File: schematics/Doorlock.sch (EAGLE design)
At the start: 40 parts, among them IC1 AT90S2313S, K1 G5V1, K2 G5V1, X1 RASPI_BOARD_B+#_H, X2 RIA182-04, X3 RIA182-07, X4 RIA182-05

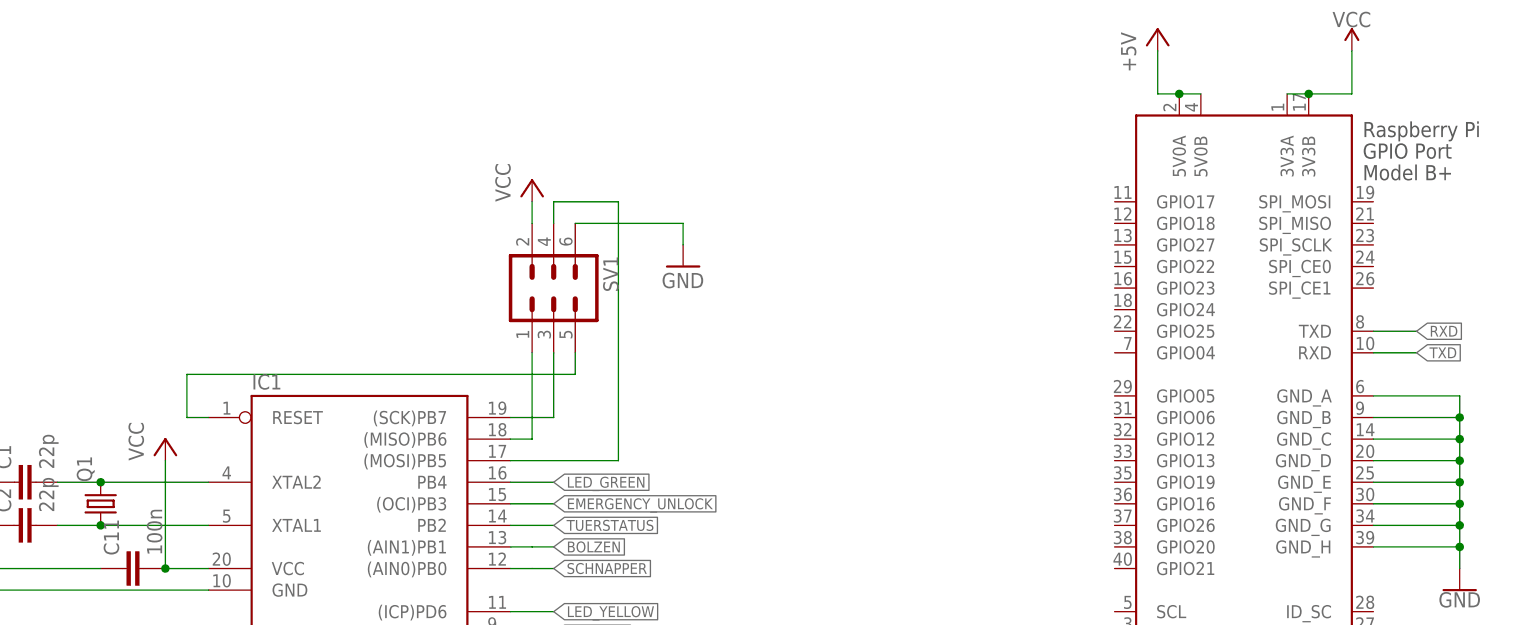
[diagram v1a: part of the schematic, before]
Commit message: Remove ISP adapter
Let's flash the device with the Raspberry Pi :-)
... But add an Jumper for the reset line.

Signed-off-by: Ralf Ramsauer <ralf@binary-kitchen.de>
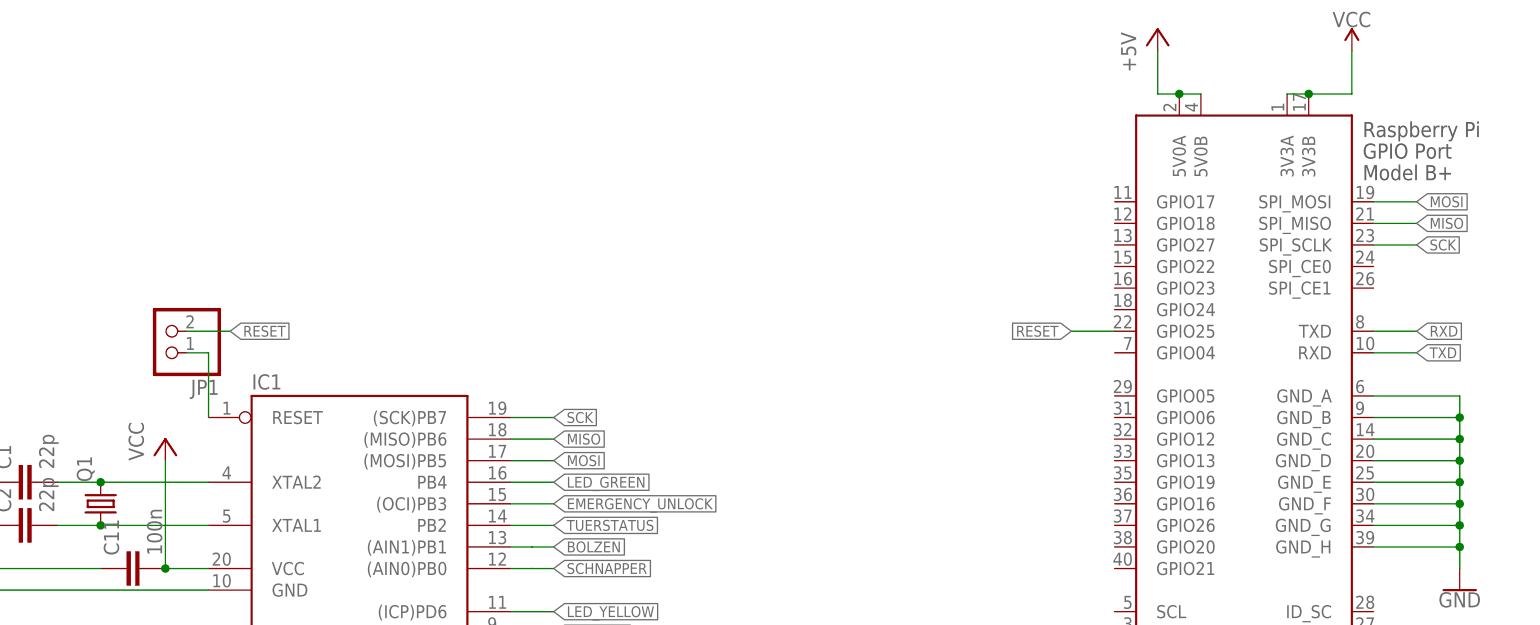
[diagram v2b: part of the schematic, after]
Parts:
- removed SV1: (no value), con-harting-ml:ML6
- added JP1: (no value), pinhead:PINHD-1X2
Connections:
- removed net N$2: IC1.(SCK)PB7, SV1.3
- removed net N$3: IC1.RESET, SV1.5
- removed net N$5: IC1.(MOSI)PB5, SV1.4
- new net MISO: IC1.(MISO)PB6, X1.SPI_MISO
- new net MOSI: IC1.(MOSI)PB5, X1.SPI_MOSI
- new net RESET: JP1.2, X1.GPIO25
- new net SCK: IC1.(SCK)PB7, X1.SPI_SCLK
- net GND: no longer SV1.6
- net N$1: now also IC1.RESET, JP1.1; no longer IC1.(MISO)PB6, SV1.1
- net VCC: no longer SV1.2
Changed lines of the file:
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@@
 <?xml version="1.0" encoding="utf-8"?>
 <!DOCTYPE eagle SYSTEM "eagle.dtd">
-<eagle version="9.1.2">
+<eagle version="9.1.3">
 <drawing>
 <settings>
@@
 <parts>
 <part name="IC1" library="atmel" deviceset="AT90S2313" device="S" value="AT90S2313S"/>
-<part name="SV1" library="con-harting-ml" deviceset="ML6" device=""/>
-<part name="GND1" library="supply1" deviceset="GND" device=""/>
-<part name="P+1" library="supply1" deviceset="VCC" device=""/>
 <part name="Q1" library="crystal" deviceset="CRYSTAL" device="HC49UP"/>
 <part name="C1" library="rcl" deviceset="C-EU" device="C0805" value="22p"/>
@@
 <part name="LED1" library="led" library_urn="urn:adsk.eagle:library:259" deviceset="LED" device="CHIP-LED0805" package3d_urn="urn:adsk.eagle:package:15818/2"/>
 <part name="LED2" library="led" library_urn="urn:adsk.eagle:library:259" deviceset="LED" device="CHIP-LED0805" package3d_urn="urn:adsk.eagle:package:15818/2"/>
+<part name="JP1" library="pinhead" library_urn="urn:adsk.eagle:library:325" deviceset="PINHD-1X2" device="" package3d_urn="urn:adsk.eagle:package:22435/2"/>
 </parts>
 <sheets>
@@
 <instances>
 <instance part="IC1" gate="G$1" x="139.7" y="144.78"/>
-<instance part="SV1" gate="1" x="162.56" y="180.34" rot="R270"/>
-<instance part="GND1" gate="1" x="177.8" y="182.88"/>
-<instance part="P+1" gate="VCC" x="160.02" y="193.04"/>
 <instance part="Q1" gate="G$1" x="109.22" y="154.94" rot="R90"/>
 <instance part="C1" gate="G$1" x="99.06" y="157.48" rot="R90"/>
@@
 <instance part="LED1" gate="G$1" x="248.92" y="119.38" rot="R270"/>
 <instance part="LED2" gate="G$1" x="248.92" y="114.3" rot="R270"/>
+<instance part="JP1" gate="G$1" x="116.84" y="175.26" rot="R180"/>
 </instances>
 <busses>
 </busses>
 <nets>
-<net name="N$1" class="0">
-<segment>
-<pinref part="IC1" gate="G$1" pin="(MISO)PB6"/>
-<pinref part="SV1" gate="1" pin="1"/>
-<wire x1="157.48" y1="162.56" x2="160.02" y2="162.56" width="0.1524" layer="91"/>
-<wire x1="160.02" y1="162.56" x2="160.02" y2="172.72" width="0.1524" layer="91"/>
-</segment>
-</net>
-<net name="N$2" class="0">
-<segment>
-<pinref part="IC1" gate="G$1" pin="(SCK)PB7"/>
-<pinref part="SV1" gate="1" pin="3"/>
-<wire x1="157.48" y1="165.1" x2="162.56" y2="165.1" width="0.1524" layer="91"/>
-<wire x1="162.56" y1="165.1" x2="162.56" y2="172.72" width="0.1524" layer="91"/>
-</segment>
-</net>
-<net name="N$3" class="0">
-<segment>
-<pinref part="IC1" gate="G$1" pin="RESET"/>
-<wire x1="121.92" y1="165.1" x2="119.38" y2="165.1" width="0.1524" layer="91"/>
-<wire x1="119.38" y1="165.1" x2="119.38" y2="170.18" width="0.1524" layer="91"/>
-<wire x1="119.38" y1="170.18" x2="165.1" y2="170.18" width="0.1524" layer="91"/>
-<wire x1="165.1" y1="170.18" x2="165.1" y2="172.72" width="0.1524" layer="91"/>
-<pinref part="SV1" gate="1" pin="5"/>
-</segment>
-</net>
 <net name="VCC" class="0">
-<segment>
-<pinref part="SV1" gate="1" pin="2"/>
-<pinref part="P+1" gate="VCC" pin="VCC"/>
-<wire x1="160.02" y1="187.96" x2="160.02" y2="190.5" width="0.1524" layer="91"/>
-</segment>
 <segment>
 <pinref part="IC1" gate="G$1" pin="VCC"/>
@@
 </net>
 <net name="GND" class="0">
-<segment>
-<pinref part="SV1" gate="1" pin="6"/>
-<wire x1="165.1" y1="187.96" x2="177.8" y2="187.96" width="0.1524" layer="91"/>
-<pinref part="GND1" gate="1" pin="GND"/>
-<wire x1="177.8" y1="187.96" x2="177.8" y2="185.42" width="0.1524" layer="91"/>
-</segment>
 <segment>
 <pinref part="C2" gate="G$1" pin="1"/>
@@
 </segment>
 </net>
-<net name="N$5" class="0">
-<segment>
-<pinref part="IC1" gate="G$1" pin="(MOSI)PB5"/>
-<wire x1="157.48" y1="160.02" x2="170.18" y2="160.02" width="0.1524" layer="91"/>
-<wire x1="170.18" y1="160.02" x2="170.18" y2="190.5" width="0.1524" layer="91"/>
-<pinref part="SV1" gate="1" pin="4"/>
-<wire x1="170.18" y1="190.5" x2="162.56" y2="190.5" width="0.1524" layer="91"/>
-<wire x1="162.56" y1="190.5" x2="162.56" y2="187.96" width="0.1524" layer="91"/>
-</segment>
-</net>
 <net name="N$6" class="0">
 <segment>
@@
 </segment>
 </net>
+<net name="MOSI" class="0">
+<segment>
+<pinref part="X1" gate="G$1" pin="SPI_MOSI"/>
+<wire x1="259.08" y1="190.5" x2="264.16" y2="190.5" width="0.1524" layer="91"/>
+<label x="264.16" y="190.5" size="1.27" layer="95" font="fixed" xref="yes"/>
+</segment>
+<segment>
+<pinref part="IC1" gate="G$1" pin="(MOSI)PB5"/>
+<wire x1="157.48" y1="160.02" x2="162.56" y2="160.02" width="0.1524" layer="91"/>
+<label x="162.56" y="160.02" size="1.27" layer="95" font="fixed" xref="yes"/>
+</segment>
+</net>
+<net name="MISO" class="0">
+<segment>
+<pinref part="X1" gate="G$1" pin="SPI_MISO"/>
+<wire x1="259.08" y1="187.96" x2="264.16" y2="187.96" width="0.1524" layer="91"/>
+<label x="264.16" y="187.96" size="1.27" layer="95" font="fixed" xref="yes"/>
+</segment>
+<segment>
+<pinref part="IC1" gate="G$1" pin="(MISO)PB6"/>
+<wire x1="157.48" y1="162.56" x2="162.56" y2="162.56" width="0.1524" layer="91"/>
+<label x="162.56" y="162.56" size="1.27" layer="95" font="fixed" xref="yes"/>
+</segment>
+</net>
+<net name="SCK" class="0">
+<segment>
+<pinref part="X1" gate="G$1" pin="SPI_SCLK"/>
+<wire x1="259.08" y1="185.42" x2="264.16" y2="185.42" width="0.1524" layer="91"/>
+<label x="264.16" y="185.42" size="1.27" layer="95" font="fixed" xref="yes"/>
+</segment>
+<segment>
+<pinref part="IC1" gate="G$1" pin="(SCK)PB7"/>
+<wire x1="157.48" y1="165.1" x2="162.56" y2="165.1" width="0.1524" layer="91"/>
+<label x="162.56" y="165.1" size="1.27" layer="95" font="fixed" xref="yes"/>
+</segment>
+</net>
+<net name="RESET" class="0">
+<segment>
+<pinref part="X1" gate="G$1" pin="GPIO25"/>
+<wire x1="228.6" y1="175.26" x2="223.52" y2="175.26" width="0.1524" layer="91"/>
+<label x="223.52" y="175.26" size="1.27" layer="95" font="fixed" rot="R180" xref="yes"/>
+</segment>
+<segment>
+<pinref part="JP1" gate="G$1" pin="2"/>
+<wire x1="119.38" y1="175.26" x2="124.46" y2="175.26" width="0.1524" layer="91"/>
+<label x="124.46" y="175.26" size="1.27" layer="95" font="fixed" xref="yes"/>
+</segment>
+</net>
+<net name="N$1" class="0">
+<segment>
+<pinref part="JP1" gate="G$1" pin="1"/>
+<wire x1="119.38" y1="172.72" x2="121.92" y2="172.72" width="0.1524" layer="91"/>
+<pinref part="IC1" gate="G$1" pin="RESET"/>
+<wire x1="121.92" y1="165.1" x2="121.92" y2="172.72" width="0.1524" layer="91"/>
+</segment>
+</net>

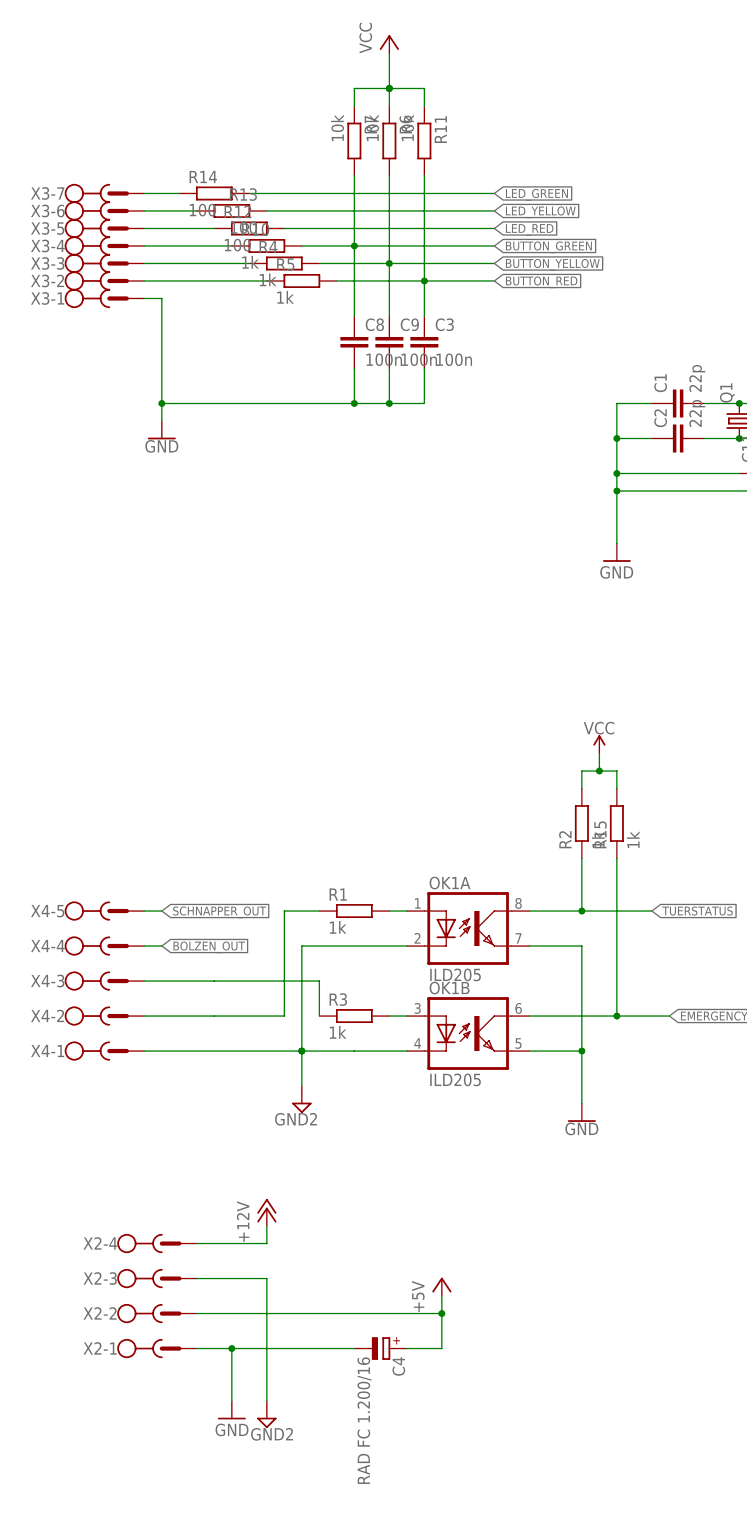
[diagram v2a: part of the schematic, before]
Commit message: schematics: improve schematics
  - Use RJ45 instead for buttons/LEDs
  - Use SMD capacitor

Signed-off-by: Ralf Ramsauer <ralf@binary-kitchen.de>
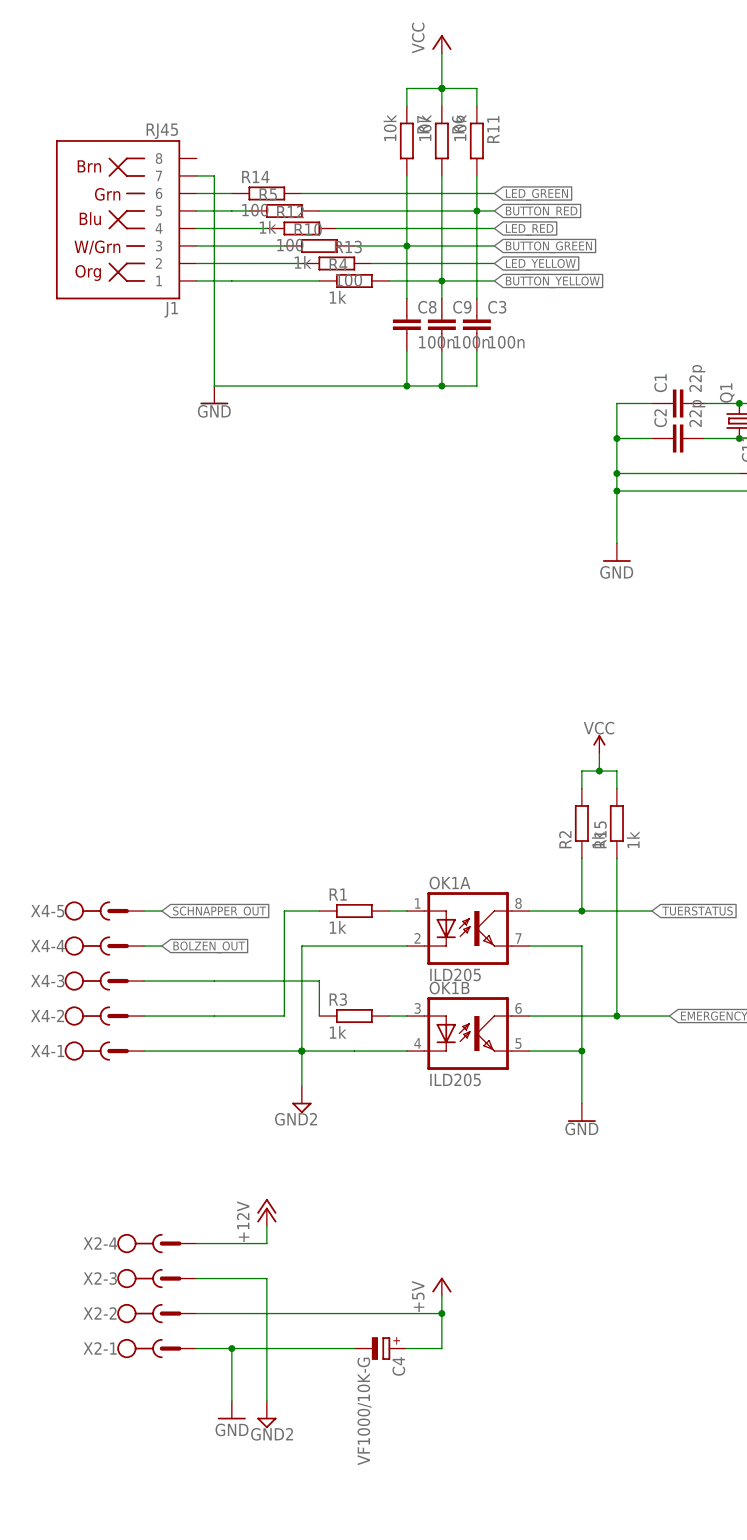
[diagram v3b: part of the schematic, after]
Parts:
- removed X3: RIA182-07, con-ria182:RIA182-07
- added J1: RJ45, SparkFun-Connectors:RJ45-8
- C4: value RAD FC 1.200/16 -> VF1000/10K-G; device rcl:CPOL-EUE5-10.5 -> rcl:CPOL-EUUD-10X10
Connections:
- removed net N$12: R14.1, X3-7.SK
- new net N$2: J1.6, R14.1
- net GND: now also J1.7; no longer X3-1.SK
- net N$11: now also J1.2; no longer X3-6.SK
- net N$20: now also J1.1; no longer X3-3.SK
- net N$21: now also J1.5; no longer X3-2.SK
- net N$8: now also J1.3; no longer X3-4.SK
- net N$9: now also J1.4; no longer X3-5.SK
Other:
- moved on the sheet: C3, C8, C9, R10, R11, R12, R13, R14, R4, R5, R6, R7
